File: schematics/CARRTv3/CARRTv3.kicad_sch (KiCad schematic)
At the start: 29 parts, among them J1 LCD_with_5_Buttons, M1 Rear Right, M2 Front Right, M3 Front Left, M4 Rear Left, M5 Lidar Servo, P1 PowerBoost_1000C, SW1 Switch, SW2 RPi0 Shutdown, SW3 Right Encoder, SW4 Left Encoder, SW5 Switch, T1 2N2222, U1 BNO055, X1 Raspberry_Pi_Zero2, X2 Raspberry_Pico2

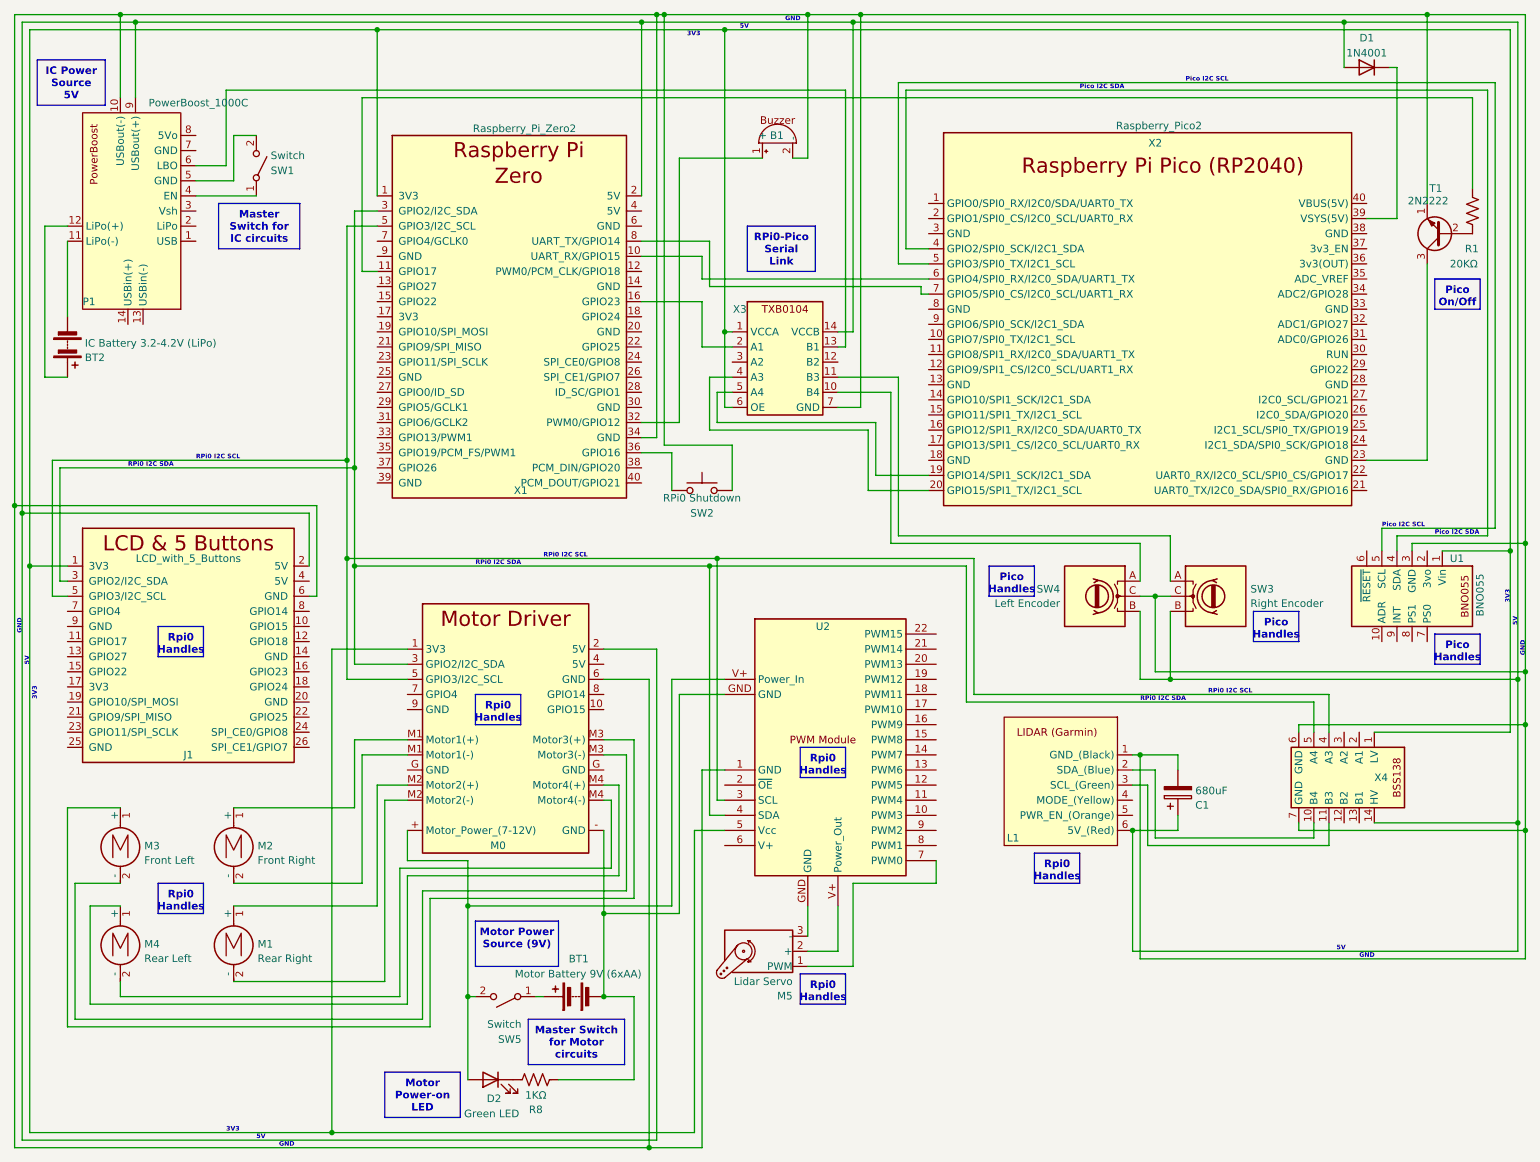
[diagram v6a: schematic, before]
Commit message: Updated schematics to reflect implementation wiring adjustments
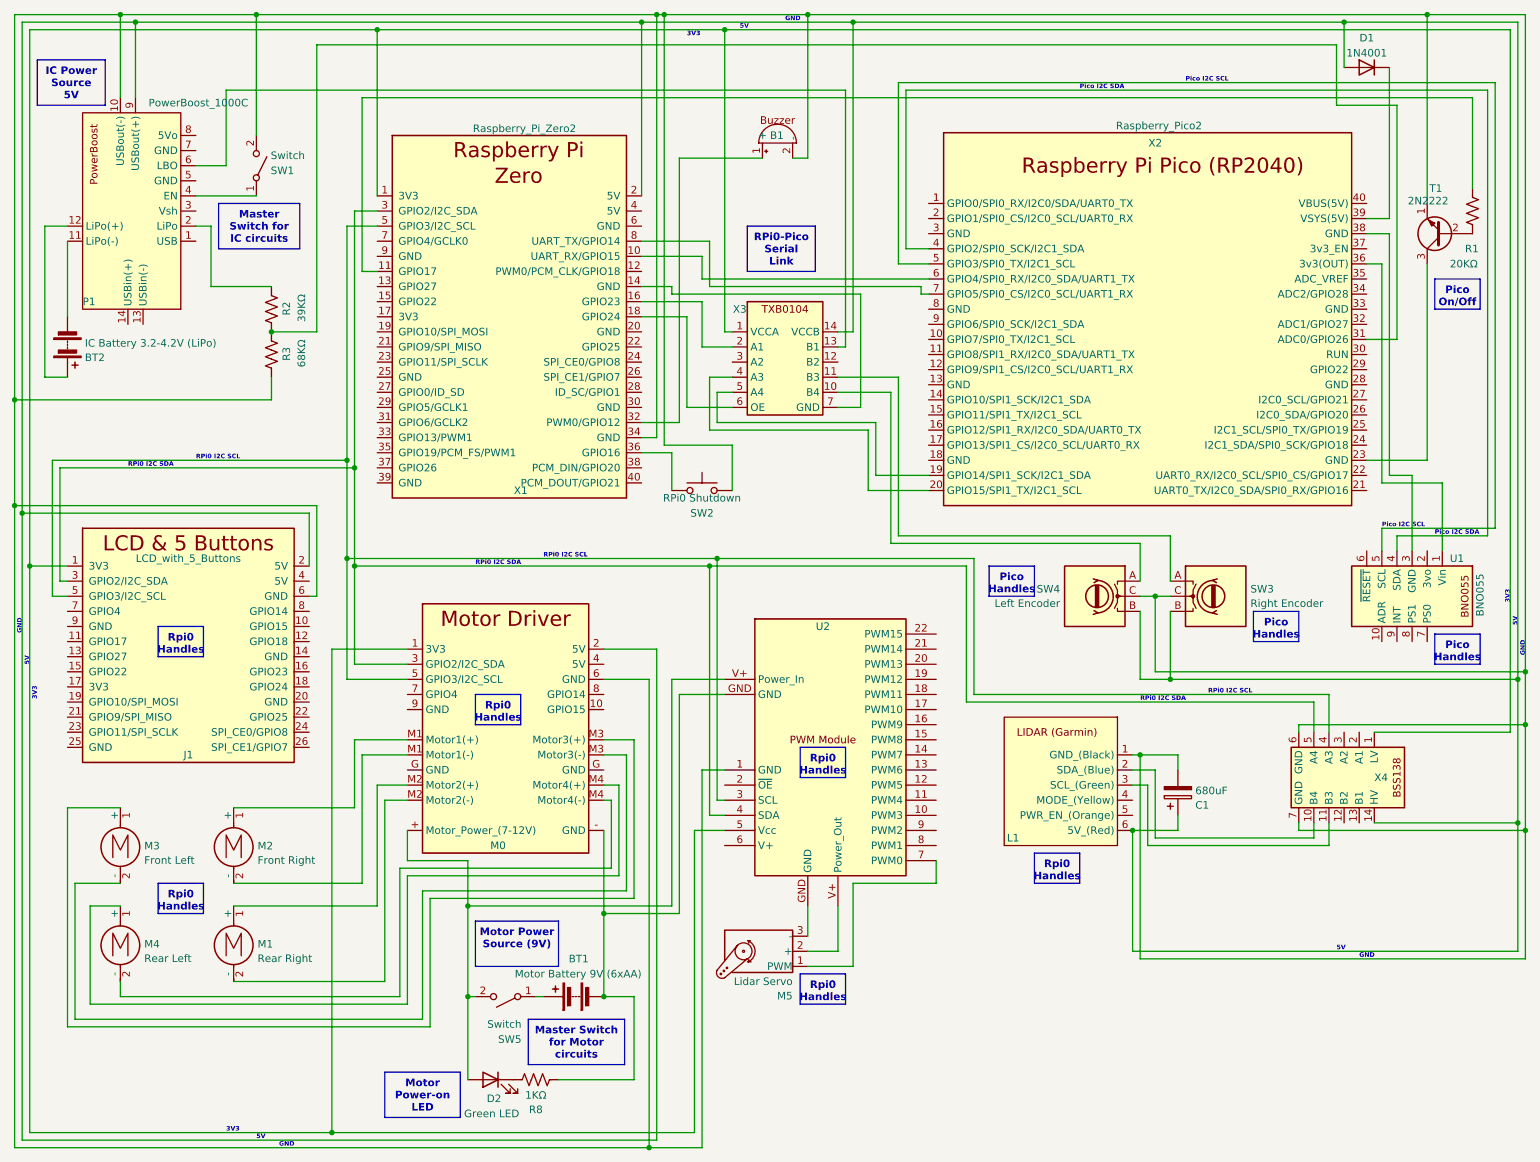
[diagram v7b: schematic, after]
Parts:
- added R2: 39KΩ, symbol Device:R_US
- added R3: 68KΩ, symbol Device:R_US
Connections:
- net at J1.1 (3V3), M0.1 (3V3), U2.5 (Vcc)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: no longer U1.1 (Vin), X3.6 (OE)
- net at B1.2 (-), C1.2, J1.6 (GND)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: now also SW1.2 (B), R3.1; no longer U1.3 (GND), X3.7 (GND)
- net at P1.2 (LiPo): now also R2.2
- net at P1.5 (GND): no longer SW1.2 (B)
- net at X1.14 (GND): now also X3.7 (GND)
- net at X1.18 (GPIO24): now also X3.6 (OE)
- net at X2.31 (ADC0/GPIO26): now also R2.1, R3.2
- net at X2.36 (3v3(OUT)): now also U1.1 (Vin)
- net at X2.38 (GND): now also U1.3 (GND)

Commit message: Reflect actual wiring of BSS138
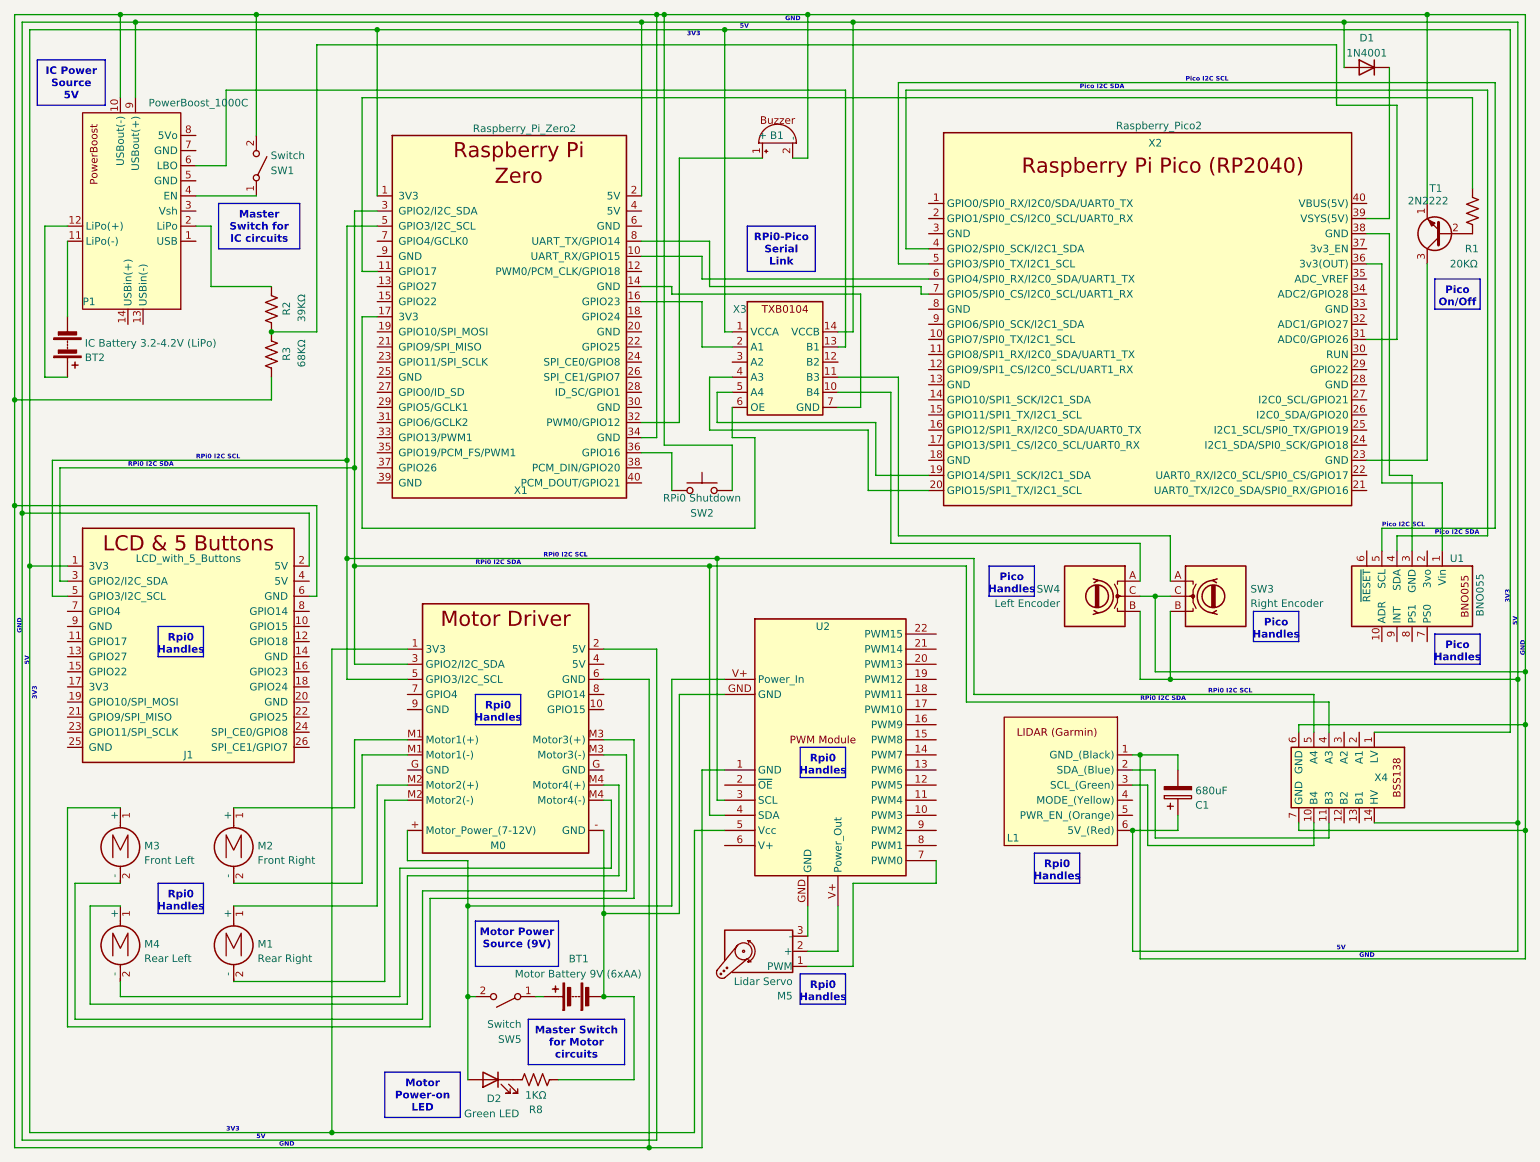
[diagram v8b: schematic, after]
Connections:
- net at X4.10 (B4): now also L1.3 (SCL_(Green)); no longer L1.2 (SDA_(Blue))
- net at X4.11 (B3): now also L1.2 (SDA_(Blue)); no longer L1.3 (SCL_(Green))
- net at J1.5 (GPIO3/I2C_SCL), M0.5 (GPIO3/I2C_SCL), U2.3 (SCL)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: now also X4.5 (A4); no longer X4.4 (A3)
- net at J1.3 (GPIO2/I2C_SDA), M0.3 (GPIO2/I2C_SDA), U2.4 (SDA)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: now also X4.4 (A3); no longer X4.5 (A4)
- net at X1.17 (3V3): now also X3.6 (OE)
- net at X1.18 (GPIO24): no longer X3.6 (OE)
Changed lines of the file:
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@@
     (stroke (width 0) (type default) (color 204 102 0 1))
   )
-  (wire (pts (xy 173.99 127) (xy 233.68 127))
+  (wire (pts (xy 173.99 127) (xy 231.14 127))
     (stroke (width 0) (type default) (color 194 194 0 1))
   )
   (wire (pts (xy 132.08 15.24) (xy 132.08 66.04))
     (stroke (width 0) (type default) (color 204 102 0 1))
+  )
+  (wire (pts (xy 203.2 152.4) (xy 231.14 152.4))
+    (stroke (width 0) (type default) (color 194 194 0 1))
   )
   (wire (pts (xy 167.64 158.75) (xy 167.64 154.94))
@@
     (stroke (width 0.2286) (type default) (color 132 0 0 1))
   )
-  (wire (pts (xy 231.14 133.35) (xy 231.14 128.27))
-    (stroke (width 0) (type default) (color 0 0 132 1))
-  )
   (wire (pts (xy 88.9 162.56) (xy 88.9 177.8))
     (stroke (width 0.2286) (type default) (color 132 0 0 1))
@@
   (wire (pts (xy 208.28 139.7) (xy 208.28 137.16))
     (stroke (width 0) (type default) (color 0 0 0 1))
+  )
+  (wire (pts (xy 231.14 148.59) (xy 231.14 152.4))
+    (stroke (width 0) (type default) (color 194 194 0 1))
   )
   (wire (pts (xy 127 149.86) (xy 127 200.66))
@@
     (stroke (width 0) (type default) (color 0 0 0 1))
   )
+  (wire (pts (xy 69.85 88.9) (xy 69.85 105.41))
+    (stroke (width 0) (type default) (color 0 0 132 1))
+  )
   (wire (pts (xy 146.05 172.72) (xy 153.67 172.72))
     (stroke (width 0) (type default))
+  )
+  (wire (pts (xy 233.68 148.59) (xy 233.68 151.13))
+    (stroke (width 0) (type default) (color 0 0 132 1))
   )
   (wire (pts (xy 245.11 67.31) (xy 245.11 27.94))
@@
     (stroke (width 0) (type default) (color 194 0 0 1))
   )
-  (wire (pts (xy 118.11 63.5) (xy 125.73 63.5))
-    (stroke (width 0) (type default) (color 194 194 194 1))
-  )
   (wire (pts (xy 250.19 12.7) (xy 250.19 44.45))
     (stroke (width 0) (type default) (color 0 0 0 1))
@@
   (wire (pts (xy 266.7 12.7) (xy 266.7 123.19))
     (stroke (width 0) (type default) (color 0 0 0 1))
+  )
+  (wire (pts (xy 133.35 78.74) (xy 133.35 83.82))
+    (stroke (width 0) (type default) (color 204 102 0 1))
   )
   (wire (pts (xy 66.04 200.66) (xy 15.24 200.66))
@@
     (stroke (width 0) (type default) (color 0 0 0 1))
   )
+  (wire (pts (xy 71.12 63.5) (xy 71.12 99.06))
+    (stroke (width 0) (type default) (color 204 102 0 1))
+  )
   (wire (pts (xy 68.58 87.63) (xy 19.05 87.63))
     (stroke (width 0) (type default) (color 194 194 0 1))
@@
     (stroke (width 0) (type default) (color 132 0 0 1))
   )
+  (wire (pts (xy 231.14 127) (xy 231.14 133.35))
+    (stroke (width 0) (type default) (color 194 194 0 1))
+  )
   (wire (pts (xy 81.28 181.61) (xy 22.86 181.61))
     (stroke (width 0.2286) (type default) (color 72 0 0 1))
@@
     (stroke (width 0.2286) (type default) (color 72 0 0 1))
   )
-  (wire (pts (xy 69.85 88.9) (xy 69.85 105.41))
-    (stroke (width 0) (type default) (color 0 0 132 1))
-  )
   (wire (pts (xy 21.59 105.41) (xy 15.24 105.41))
     (stroke (width 0) (type default) (color 204 102 0 1))
@@
     (stroke (width 0) (type default) (color 194 194 0 1))
   )
-  (wire (pts (xy 233.68 148.59) (xy 233.68 152.4))
-    (stroke (width 0) (type default) (color 194 194 0 1))
-  )
   (wire (pts (xy 69.85 134.62) (xy 78.74 134.62))
     (stroke (width 0.2286) (type default) (color 132 0 0 1))
@@
     (stroke (width 0) (type default))
   )
-  (wire (pts (xy 204.47 151.13) (xy 231.14 151.13))
+  (wire (pts (xy 204.47 151.13) (xy 233.68 151.13))
     (stroke (width 0) (type default) (color 0 0 132 1))
   )
@@
     (stroke (width 0) (type default))
   )
-  (wire (pts (xy 172.72 128.27) (xy 231.14 128.27))
+  (wire (pts (xy 172.72 128.27) (xy 233.68 128.27))
     (stroke (width 0) (type default) (color 0 0 132 1))
   )
@@
     (stroke (width 0) (type default))
   )
-  (wire (pts (xy 233.68 133.35) (xy 233.68 127))
-    (stroke (width 0) (type default) (color 194 194 0 1))
-  )
   (wire (pts (xy 266.7 12.7) (xy 250.19 12.7))
     (stroke (width 0) (type default) (color 0 0 0 1))
@@
     (stroke (width 0.2286) (type default) (color 132 0 0 1))
   )
+  (wire (pts (xy 71.12 63.5) (xy 73.66 63.5))
+    (stroke (width 0) (type default) (color 204 102 0 1))
+  )
   (wire (pts (xy 82.55 161.29) (xy 82.55 182.88))
     (stroke (width 0.2286) (type default) (color 132 0 0 1))
@@
     (stroke (width 0) (type default) (color 0 0 0 1))
   )
-  (wire (pts (xy 203.2 152.4) (xy 233.68 152.4))
-    (stroke (width 0) (type default) (color 194 194 0 1))
-  )
   (wire (pts (xy 133.35 73.66) (xy 129.54 73.66))
     (stroke (width 0) (type default))
@@
     (stroke (width 0) (type default) (color 0 0 0 1))
   )
-  (wire (pts (xy 125.73 78.74) (xy 125.73 63.5))
-    (stroke (width 0) (type default) (color 194 194 194 1))
-  )
   (wire (pts (xy 62.23 105.41) (xy 62.23 96.52))
     (stroke (width 0) (type default) (color 194 0 0 1))
@@
   (wire (pts (xy 161.29 24.13) (xy 261.62 24.13))
     (stroke (width 0) (type default) (color 194 194 0 1))
+  )
+  (wire (pts (xy 133.35 83.82) (xy 137.16 83.82))
+    (stroke (width 0) (type default) (color 204 102 0 1))
   )
   (wire (pts (xy 73.66 55.88) (xy 71.12 55.88))
@@
     (stroke (width 0.2286) (type default) (color 132 0 0 1))
   )
-  (wire (pts (xy 125.73 78.74) (xy 133.35 78.74))
-    (stroke (width 0) (type default) (color 194 194 194 1))
-  )
   (wire (pts (xy 78.74 137.16) (xy 71.12 137.16))
     (stroke (width 0.2286) (type default) (color 72 0 0 1))
@@
     (stroke (width 0) (type default) (color 0 0 132 1))
   )
+  (wire (pts (xy 233.68 128.27) (xy 233.68 133.35))
+    (stroke (width 0) (type default) (color 0 0 132 1))
+  )
   (wire (pts (xy 120.65 201.93) (xy 13.97 201.93))
     (stroke (width 0) (type default) (color 194 0 0 1))
@@
   (wire (pts (xy 242.57 99.06) (xy 261.62 99.06))
     (stroke (width 0) (type default) (color 194 194 0 1))
+  )
+  (wire (pts (xy 137.16 83.82) (xy 137.16 99.06))
+    (stroke (width 0) (type default) (color 204 102 0 1))
   )
   (wire (pts (xy 22.86 181.61) (xy 22.86 158.75))
@@
     (stroke (width 0) (type default) (color 194 0 0 1))
   )
+  (wire (pts (xy 71.12 99.06) (xy 137.16 99.06))
+    (stroke (width 0) (type default) (color 204 102 0 1))
+  )
   (wire (pts (xy 88.9 162.56) (xy 88.9 154.94))
     (stroke (width 0.2286) (type default) (color 132 0 0 1))
@@
     (stroke (width 0) (type default))
   )
-  (wire (pts (xy 231.14 151.13) (xy 231.14 148.59))
-    (stroke (width 0) (type default) (color 0 0 132 1))
-  )
   (text_box "Rpi0 Handles"
